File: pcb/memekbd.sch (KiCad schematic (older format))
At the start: 196 parts, among them J1 AudioJack4, J2 AudioJack4, SW1 SW_Push, SW10 SW_Push, SW11 SW_Push, SW12 SW_Push, SW13 SW_Push, SW14 SW_Push, SW15 SW_Push, SW16 SW_Push, SW17 SW_Push, SW18 SW_Push, SW19 SW_Push, SW2 SW_Push, SW20 SW_Push, SW21 SW_Push, SW22 SW_Push, SW23 SW_Push, SW24 SW_Push, SW25 SW_Push, SW26 SW_Push, SW27 SW_Push, SW28 SW_Push, SW29 SW_Push, SW3 SW_Push, SW30 SW_Push, SW31 SW_Push, SW32 SW_Push, SW33 SW_Push, SW34 SW_Push, SW35 SW_Push, SW36 SW_Push, SW37 SW_Push, SW38 SW_Push, SW39 SW_Push, SW4 SW_Push, SW40 SW_Push, SW41 SW_Push, SW42 SW_Push, SW43 SW_Push, SW44 SW_Push, SW45 SW_Push, SW46 SW_Push, SW47 SW_Push, SW48 SW_Push, SW5 SW_Push, SW6 SW_Push, SW7 SW_Push, SW8 SW_Push, SW9 SW_Push, U1 ProMicro, U2 ProMicro

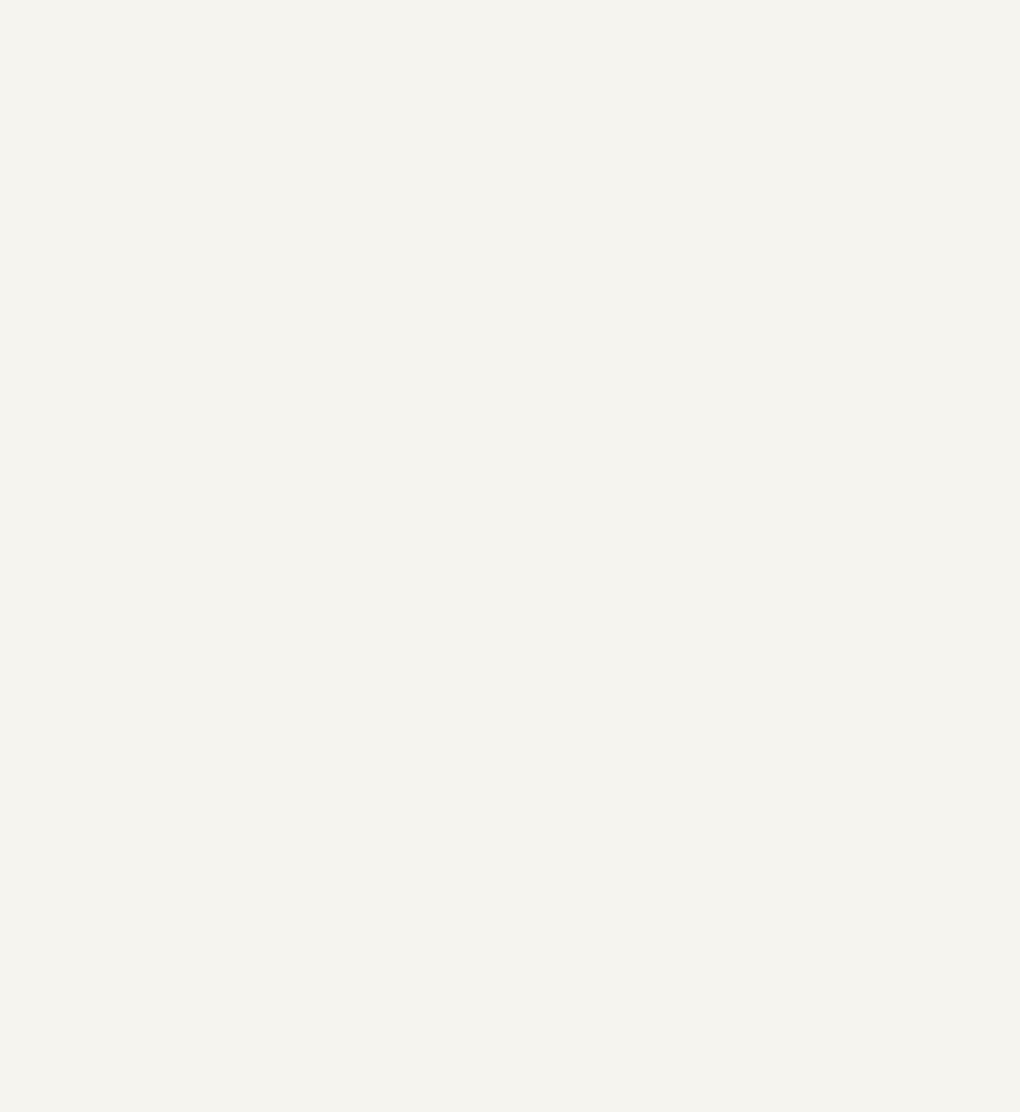
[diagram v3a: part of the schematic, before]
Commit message: Mounting holes in schematic.
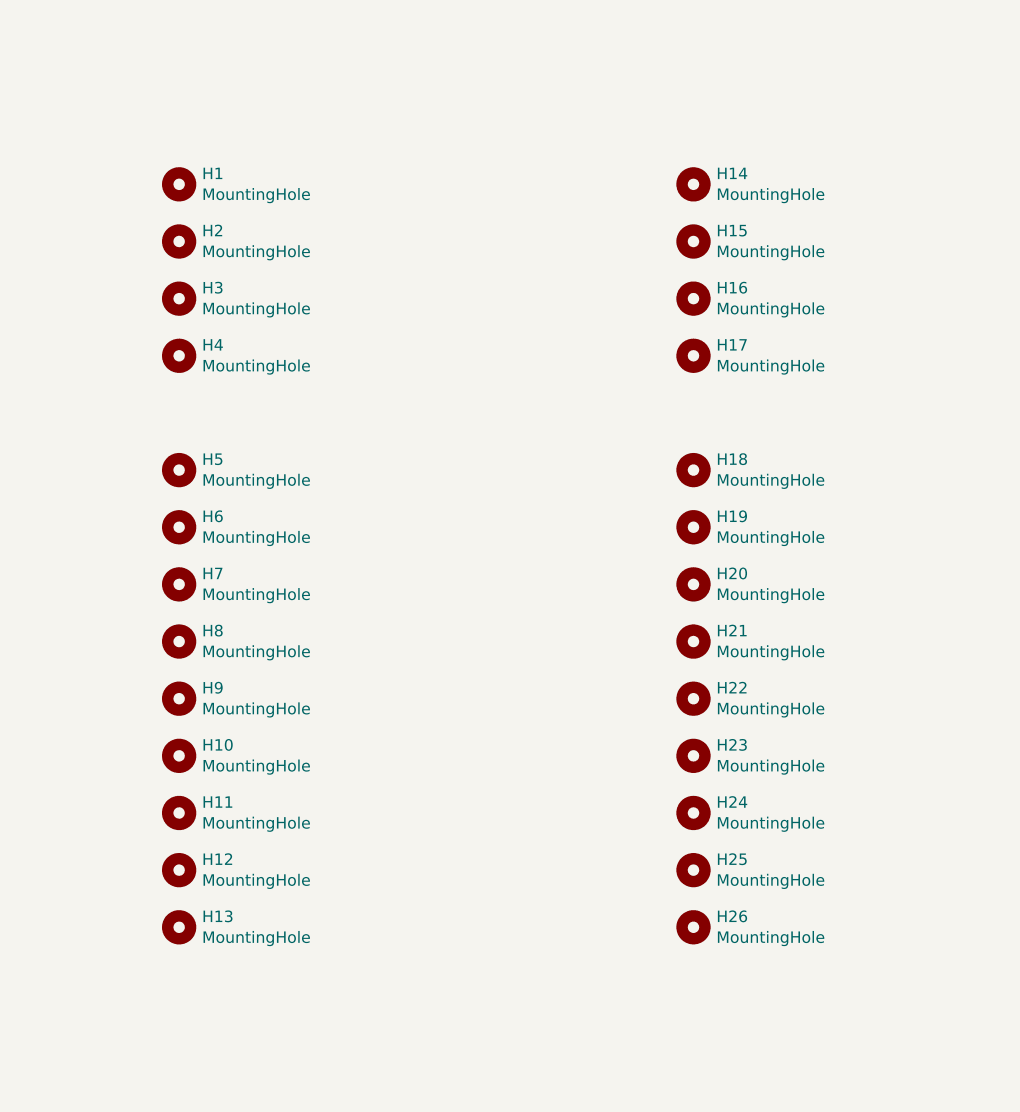
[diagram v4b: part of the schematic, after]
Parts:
- added H1, H14, H15, H16, H17, H2, H3, H4: MountingHole, MountingHole:MountingHole_5.3mm_M5_ISO7380, symbol Mechanical:MountingHole
- added H10, H11, H12, H13, H18, H19, H20, H21, H22, H23, H24, H25, H26, H5, H6, H7, H8, H9: MountingHole, MountingHole:MountingHole_3.2mm_M3_ISO7380, symbol Mechanical:MountingHole

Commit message: Fix bug...
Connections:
- net at LED5.4 (DIN): now also R5.1; no longer LED1.4 (DIN)
- net at LED15.2 (DOUT): now also LED1.4 (DIN); no longer R5.1
- net at LED20.2 (DOUT): now also LED2.4 (DIN); no longer LED21.2 (DOUT)
- net at LED3.4 (DIN): now also LED21.2 (DOUT); no longer LED2.4 (DIN)
- net at LED22.2 (DOUT): now also LED4.4 (DIN); no longer LED23.2 (DOUT)
- net at LED24.4 (DIN): now also LED38.2 (DOUT); no longer LED25.4 (DIN)
- net at LED43.2 (DOUT): now also LED25.4 (DIN); no longer LED38.2 (DOUT)
- net at LED44.2 (DOUT): now also LED26.4 (DIN); no longer LED45.2 (DOUT)
- net at LED27.4 (DIN): now also LED45.2 (DOUT); no longer LED26.4 (DIN)
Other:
- moved on the sheet: R5
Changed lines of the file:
@@
 	4100 8500 4500 8500
 Wire Wire Line
-	6100 8500 6500 8500
-Wire Wire Line
-	6100 10000 6500 10000
-Wire Wire Line
 	8600 7000 9000 7000
-Wire Wire Line
-	12600 10000 13000 10000
-Wire Wire Line
-	12600 11500 13000 11500
 NoConn ~ 12600 13000
 $Comp
@@
 Text Label 18100 3650 0    50   ~ 0
 rSCL
-Text Label 6100 7000 0    50   ~ 0
+Text Label 1700 7000 2    50   ~ 0
 lLED
 Text Label 8300 7000 2    50   ~ 0
@@
 	1    0    0    -1
 $EndComp
-Wire Wire Line
-	12600 8500 13000 8500
 $Comp
 L power:GND #PWR023
@@
 L Device:R R5
 U 1 1 60E55CD7
-P 5950 7000
-F 0 "R5" V 5743 7000 50  0000 C CNN
-F 1 "1k" V 5834 7000 50  0000 C CNN
-F 2 "Resistor_THT:R_Axial_DIN0207_L6.3mm_D2.5mm_P7.62mm_Horizontal" V 5880 7000 50  0001 C CNN
-F 3 "~" H 5950 7000 50  0001 C CNN
-	1    5950 7000
-	0    -1   -1   0
+P 1850 7000
+F 0 "R5" V 1643 7000 50  0000 C CNN
+F 1 "1k" V 1734 7000 50  0000 C CNN
+F 2 "Resistor_THT:R_Axial_DIN0207_L6.3mm_D2.5mm_P7.62mm_Horizontal" V 1780 7000 50  0001 C CNN
+F 3 "~" H 1850 7000 50  0001 C CNN
+	1    1850 7000
+	0    1    1    0
 $EndComp
 $Comp
@@
 	0    1    1    0
 $EndComp
-Wire Wire Line
-	5800 7000 5100 7000
-Wire Wire Line
-	2500 7000 1500 7000
-Wire Wire Line
-	1500 7000 1500 8500
-Wire Wire Line
-	6500 8500 6500 10000
-Wire Wire Line
-	1500 10000 1500 11500
-NoConn ~ 1500 13000
-Wire Wire Line
-	6250 11500 6250 13000
-Wire Wire Line
-	6250 13000 6100 13000
-Wire Wire Line
-	6100 11500 6250 11500
-Wire Wire Line
-	13000 7000 13000 8500
-Wire Wire Line
-	11600 7000 13000 7000
-Wire Wire Line
-	8000 8500 8000 10000
-Wire Wire Line
-	13000 10000 13000 11500
-Wire Wire Line
-	8000 11500 8000 13000
 $Comp
 L Mechanical:MountingHole H1
@@
 	1    0    0    -1
 $EndComp
+Wire Wire Line
+	2000 7000 2500 7000
+Wire Wire Line
+	5100 7000 5100 7750
+Wire Wire Line
+	5100 7750 1500 7750
+Wire Wire Line
+	1500 7750 1500 8500
+Wire Wire Line
+	6100 8500 6100 9375
+Wire Wire Line
+	6100 9375 1500 9375
+Wire Wire Line
+	1500 9375 1500 10000
+Wire Wire Line
+	6100 10000 6100 10725
+Wire Wire Line
+	6100 10725 1500 10725
+Wire Wire Line
+	1500 10725 1500 11500
+Wire Wire Line
+	6100 11500 6100 12200
+Wire Wire Line
+	6100 12200 1500 12200
+Wire Wire Line
+	1500 12200 1500 13000
+NoConn ~ 6100 13000
+Wire Wire Line
+	11600 7000 11600 8025
+Wire Wire Line
+	11600 8025 8000 8025
+Wire Wire Line
+	8000 8025 8000 8500
+Wire Wire Line
+	12600 8500 12600 9300
+Wire Wire Line
+	12600 9300 8000 9300
+Wire Wire Line
+	8000 9300 8000 10000
+Wire Wire Line
+	12600 10000 12600 10725
+Wire Wire Line
+	12600 10725 8000 10725
+Wire Wire Line
+	8000 10725 8000 11500
+Wire Wire Line
+	12600 11500 12600 12250
+Wire Wire Line
+	12600 12250 8000 12250
+Wire Wire Line
+	8000 12250 8000 13000
 $EndSCHEMATC
